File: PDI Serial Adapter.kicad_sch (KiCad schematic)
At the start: 7 parts, among them J1 2.54, J2 1.27, J3 PROG, J4 FTDI, J5 FTDI_VCC, J6 DTR_RST, J7 TARGET_PWR

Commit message: Removed RX/TX from programmer header
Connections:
- net MCU_RX: no longer J3.3 (Pin_3)
- net MCU_TX: no longer J3.4 (Pin_4)
- no-connect marks 1 -> 3
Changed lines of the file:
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@@
     (comment 2 "Licence: GPLv3")
   )
+  (no_connect (at 95.25 88.9))
   (no_connect (at 135.89 68.58))
+  (no_connect (at 107.95 88.9))
   (wire (pts (xy 127 76.2) (xy 135.89 76.2))
     (stroke (width 0) (type default))
@@
     (stroke (width 0) (type default))
   )
-  (wire (pts (xy 86.36 88.9) (xy 95.25 88.9))
-    (stroke (width 0) (type default))
-  )
   (wire (pts (xy 107.95 86.36) (xy 116.84 86.36))
     (stroke (width 0) (type default))
@@
   )
   (wire (pts (xy 107.95 54.61) (xy 116.84 54.61))
-    (stroke (width 0) (type default))
-  )
-  (wire (pts (xy 107.95 88.9) (xy 116.84 88.9))
     (stroke (width 0) (type default))
   )
@@
     (effects (font (size 1.27 1.27)) (justify left bottom))
   )
-  (label "MCU_TX" (at 116.84 88.9 180) (fields_autoplaced)
-    (effects (font (size 1.27 1.27)) (justify right bottom))
-  )
   (label "VCC" (at 116.84 54.61 180) (fields_autoplaced)
     (effects (font (size 1.27 1.27)) (justify right bottom))
@@
     (effects (font (size 1.27 1.27)) (justify left bottom))
   )
-  (label "MCU_RX" (at 86.36 88.9 0) (fields_autoplaced)
-    (effects (font (size 1.27 1.27)) (justify left bottom))
-  )

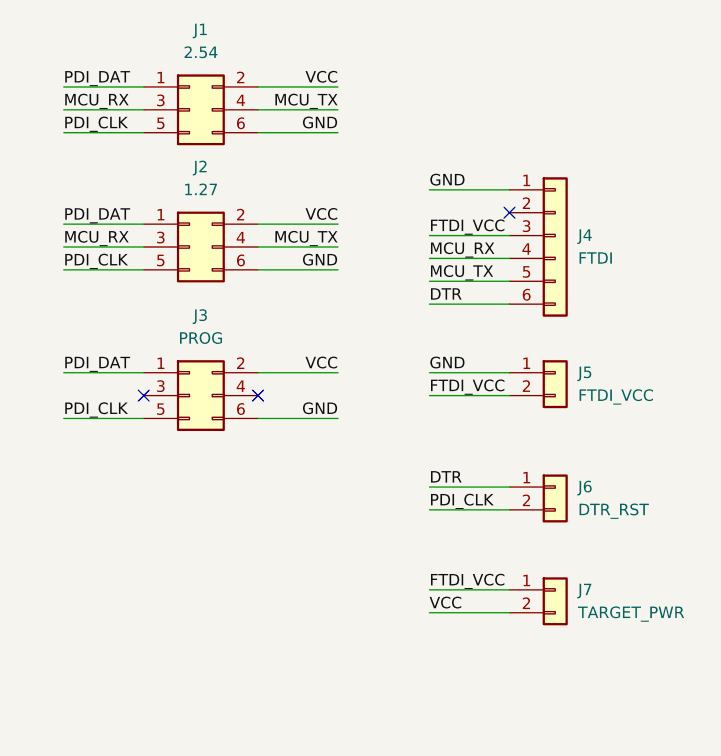
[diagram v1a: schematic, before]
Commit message: Open drain for DTR reset
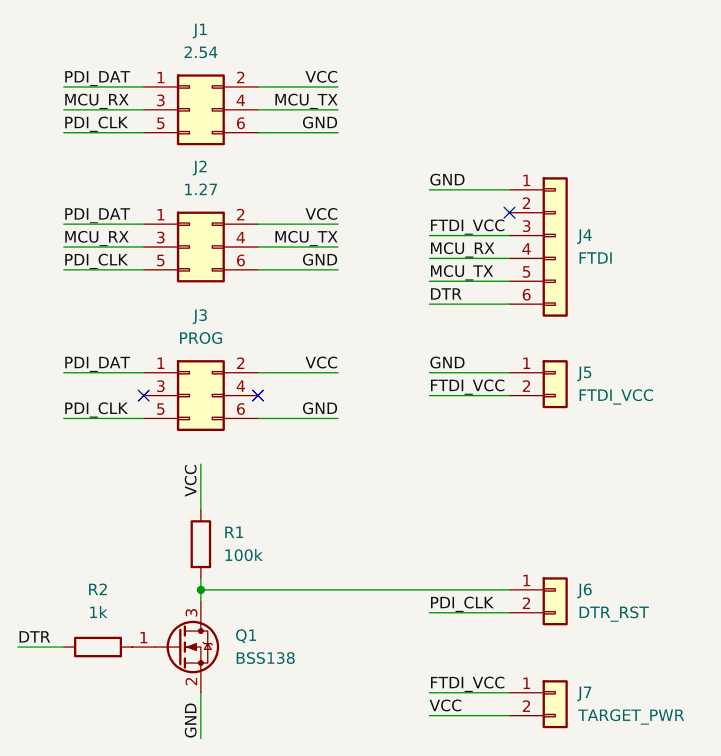
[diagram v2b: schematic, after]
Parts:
- added Q1: BSS138, Package_TO_SOT_SMD:SOT-23, symbol Transistor_FET:BSS138
- added R1: 100k, Resistor_SMD:R_0805_2012Metric_Pad1.20x1.40mm_HandSolder, symbol Device:R
- added R2: 1k, Resistor_SMD:R_0805_2012Metric_Pad1.20x1.40mm_HandSolder, symbol Device:R
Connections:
- net DTR: now also R2.1; no longer J6.1 (Pin_1)
- net GND: now also Q1.2 (S)
- net VCC: now also R1.1
- new net: J6.1 (Pin_1), Q1.3 (D), R1.2
- new net: Q1.1 (G), R2.2
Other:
- moved on the sheet: J6, J7
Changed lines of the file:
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@@
     (comment 2 "Licence: GPLv3")
+  )
+  (junction (at 101.6 110.49) (diameter 0) (color 0 0 0 0)
   )
   (no_connect (at 95.25 88.9))
@@
     (stroke (width 0) (type default))
   )
-  (wire (pts (xy 127 99.06) (xy 135.89 99.06))
-    (stroke (width 0) (type default))
-  )
   (wire (pts (xy 107.95 72.39) (xy 116.84 72.39))
     (stroke (width 0) (type default))
@@
     (stroke (width 0) (type default))
   )
+  (wire (pts (xy 81.28 116.84) (xy 86.36 116.84))
+    (stroke (width 0) (type default))
+  )
   (wire (pts (xy 86.36 57.15) (xy 95.25 57.15))
     (stroke (width 0) (type default))
@@
     (stroke (width 0) (type default))
   )
-  (wire (pts (xy 127 110.49) (xy 135.89 110.49))
+  (wire (pts (xy 127 121.92) (xy 135.89 121.92))
     (stroke (width 0) (type default))
   )
@@
     (stroke (width 0) (type default))
   )
+  (wire (pts (xy 101.6 110.49) (xy 101.6 111.76))
+    (stroke (width 0) (type default))
+  )
   (wire (pts (xy 127 66.04) (xy 135.89 66.04))
     (stroke (width 0) (type default))
@@
     (stroke (width 0) (type default))
   )
+  (wire (pts (xy 101.6 121.92) (xy 101.6 127))
+    (stroke (width 0) (type default))
+  )
+  (wire (pts (xy 101.6 109.22) (xy 101.6 110.49))
+    (stroke (width 0) (type default))
+  )
   (wire (pts (xy 127 78.74) (xy 135.89 78.74))
     (stroke (width 0) (type default))
   )
+  (wire (pts (xy 101.6 96.52) (xy 101.6 101.6))
+    (stroke (width 0) (type default))
+  )
   (wire (pts (xy 86.36 74.93) (xy 95.25 74.93))
     (stroke (width 0) (type default))
@@
     (stroke (width 0) (type default))
   )
+  (wire (pts (xy 127 124.46) (xy 135.89 124.46))
+    (stroke (width 0) (type default))
+  )
   (wire (pts (xy 127 113.03) (xy 135.89 113.03))
     (stroke (width 0) (type default))
   )
-  (wire (pts (xy 127 101.6) (xy 135.89 101.6))
+  (wire (pts (xy 101.6 110.49) (xy 135.89 110.49))
     (stroke (width 0) (type default))
   )
@@
     (effects (font (size 1.27 1.27)) (justify right bottom))
   )
-  (label "PDI_CLK" (at 127 101.6 0) (fields_autoplaced)
-    (effects (font (size 1.27 1.27)) (justify left bottom))
-  )
-  (label "DTR" (at 127 99.06 0) (fields_autoplaced)
+  (label "PDI_CLK" (at 127 113.03 0) (fields_autoplaced)
+    (effects (font (size 1.27 1.27)) (justify left bottom))
+  )
+  (label "DTR" (at 81.28 116.84 0) (fields_autoplaced)
     (effects (font (size 1.27 1.27)) (justify left bottom))
   )
@@
     (effects (font (size 1.27 1.27)) (justify left bottom))
   )
+  (label "GND" (at 101.6 127 90) (fields_autoplaced)
+    (effects (font (size 1.27 1.27)) (justify left bottom))
+  )
   (label "GND" (at 116.84 74.93 180) (fields_autoplaced)
     (effects (font (size 1.27 1.27)) (justify right bottom))
@@
     (effects (font (size 1.27 1.27)) (justify left bottom))
   )
+  (label "VCC" (at 101.6 96.52 270) (fields_autoplaced)
+    (effects (font (size 1.27 1.27)) (justify right bottom))
+  )
   (label "MCU_TX" (at 116.84 72.39 180) (fields_autoplaced)
     (effects (font (size 1.27 1.27)) (justify right bottom))
@@
     (effects (font (size 1.27 1.27)) (justify right bottom))
   )
-  (label "FTDI_VCC" (at 127 110.49 0) (fields_autoplaced)
-    (effects (font (size 1.27 1.27)) (justify left bottom))
-  )
-  (label "VCC" (at 127 113.03 0) (fields_autoplaced)
+  (label "FTDI_VCC" (at 127 121.92 0) (fields_autoplaced)
+    (effects (font (size 1.27 1.27)) (justify left bottom))
+  )
+  (label "VCC" (at 127 124.46 0) (fields_autoplaced)
     (effects (font (size 1.27 1.27)) (justify left bottom))
   )
   (label "GND" (at 127 86.36 0) (fields_autoplaced)
     (effects (font (size 1.27 1.27)) (justify left bottom))
+  )
+  (symbol (lib_id "Device:R") (at 101.6 105.41 0) (unit 1)
+    (in_bom yes) (on_board yes) (dnp no) (fields_autoplaced)
+    (property "Reference" "R1" (at 104.14 104.14 0)
+      (effects (font (size 1.27 1.27)) (justify left))
+    )
+    (property "Value" "100k" (at 104.14 106.68 0)
+      (effects (font (size 1.27 1.27)) (justify left))
+    )
+    (property "Footprint" "Resistor_SMD:R_0805_2012Metric_Pad1.20x1.40mm_HandSolder" (at 99.822 105.41 90)
+      (effects (font (size 1.27 1.27)) hide)
+    )
+    (property "Datasheet" "~" (at 101.6 105.41 0)
+      (effects (font (size 1.27 1.27)) hide)
+    )
+    (pin "1")
+    (pin "2")
+    (instances
+      (project "PDI Serial Adapter"
+        (path "/53f06091-c417-4bfd-9c07-d86260f24dc3"
+          (reference "R1") (unit 1)
+        )
+      )
+    )
   )
   (symbol (lib_id "Connector_Generic:Conn_02x03_Odd_Even") (at 100.33 57.15 0) (unit 1)
@@
     )
   )
+  (symbol (lib_id "Device:R") (at 90.17 116.84 90) (unit 1)
+    (in_bom yes) (on_board yes) (dnp no) (fields_autoplaced)
+    (property "Reference" "R2" (at 90.17 110.49 90)
+      (effects (font (size 1.27 1.27)))
+    )
+    (property "Value" "1k" (at 90.17 113.03 90)
+      (effects (font (size 1.27 1.27)))
+    )
+    (property "Footprint" "Resistor_SMD:R_0805_2012Metric_Pad1.20x1.40mm_HandSolder" (at 90.17 118.618 90)
+      (effects (font (size 1.27 1.27)) hide)
+    )
+    (property "Datasheet" "~" (at 90.17 116.84 0)
+      (effects (font (size 1.27 1.27)) hide)
+    )
+    (pin "1")
+    (pin "2")
+    (instances
+      (project "PDI Serial Adapter"
+        (path "/53f06091-c417-4bfd-9c07-d86260f24dc3"
+          (reference "R2") (unit 1)
+        )
+      )
+    )
+  )
+  (symbol (lib_id "Transistor_FET:BSS138") (at 99.06 116.84 0) (unit 1)
+    (in_bom yes) (on_board yes) (dnp no) (fields_autoplaced)
+    (property "Reference" "Q1" (at 105.41 115.57 0)
+      (effects (font (size 1.27 1.27)) (justify left))
+    )
+    (property "Value" "BSS138" (at 105.41 118.11 0)
+      (effects (font (size 1.27 1.27)) (justify left))
+    )
+    (property "Footprint" "Package_TO_SOT_SMD:SOT-23" (at 104.14 118.745 0)
+      (effects (font (size 1.27 1.27) italic) (justify left) hide)
+    )
+    (property "Datasheet" "https://www.onsemi.com/pub/Collateral/BSS138-D.PDF" (at 99.06 116.84 0)
+      (effects (font (size 1.27 1.27)) (justify left) hide)
+    )
+    (pin "1")
+    (pin "2")
+    (pin "3")
+    (instances
+      (project "PDI Serial Adapter"
+        (path "/53f06091-c417-4bfd-9c07-d86260f24dc3"
+          (reference "Q1") (unit 1)
+        )
+      )
+    )
+  )
   (symbol (lib_id "Connector_Generic:Conn_02x03_Odd_Even") (at 100.33 72.39 0) (unit 1)
     (in_bom yes) (on_board yes) (dnp no) (fields_autoplaced)
@@
     )
   )
-  (symbol (lib_id "Connector_Generic:Conn_01x02") (at 140.97 99.06 0) (unit 1)
-    (in_bom yes) (on_board yes) (dnp no) (fields_autoplaced)
-    (property "Reference" "J6" (at 143.51 99.06 0)
-      (effects (font (size 1.27 1.27)) (justify left))
-    )
-    (property "Value" "DTR_RST" (at 143.51 101.6 0)
-      (effects (font (size 1.27 1.27)) (justify left))
-    )
-    (property "Footprint" "Connector_PinHeader_2.54mm:PinHeader_1x02_P2.54mm_Vertical" (at 140.97 99.06 0)
-      (effects (font (size 1.27 1.27)) hide)
-    )
-    (property "Datasheet" "~" (at 140.97 99.06 0)
+  (symbol (lib_id "Connector_Generic:Conn_01x02") (at 140.97 110.49 0) (unit 1)
+    (in_bom yes) (on_board yes) (dnp no) (fields_autoplaced)
+    (property "Reference" "J6" (at 143.51 110.49 0)
+      (effects (font (size 1.27 1.27)) (justify left))
+    )
+    (property "Value" "DTR_RST" (at 143.51 113.03 0)
+      (effects (font (size 1.27 1.27)) (justify left))
+    )
+    (property "Footprint" "Connector_PinHeader_2.54mm:PinHeader_1x02_P2.54mm_Vertical" (at 140.97 110.49 0)
+      (effects (font (size 1.27 1.27)) hide)
+    )
+    (property "Datasheet" "~" (at 140.97 110.49 0)
       (effects (font (size 1.27 1.27)) hide)
     )
@@
     )
   )
-  (symbol (lib_id "Connector_Generic:Conn_01x02") (at 140.97 110.49 0) (unit 1)
-    (in_bom yes) (on_board yes) (dnp no) (fields_autoplaced)
-    (property "Reference" "J7" (at 143.51 110.49 0)
-      (effects (font (size 1.27 1.27)) (justify left))
-    )
-    (property "Value" "TARGET_PWR" (at 143.51 113.03 0)
-      (effects (font (size 1.27 1.27)) (justify left))
-    )
-    (property "Footprint" "Connector_PinHeader_2.54mm:PinHeader_1x02_P2.54mm_Vertical" (at 140.97 110.49 0)
-      (effects (font (size 1.27 1.27)) hide)
-    )
-    (property "Datasheet" "~" (at 140.97 110.49 0)
-      (effects (font (size 1.27 1.27)) hide)
-    )
+  (symbol (lib_id "Connector_Generic:Conn_01x02") (at 140.97 121.92 0) (unit 1)
+    (in_bom yes) (on_board yes) (dnp no) (fields_autoplaced)
+    (property "Reference" "J7" (at 143.51 121.92 0)
+      (effects (font (size 1.27 1.27)) (justify left))
+    )
+    (property "Value" "TARGET_PWR" (at 143.51 124.46 0)
+      (effects (font (size 1.27 1.27)) (justify left))
+    )
+    (property "Footprint" "Connector_PinHeader_2.54mm:PinHeader_1x02_P2.54mm_Vertical" (at 140.97 121.92 0)
+      (effects (font (size 1.27 1.27)) hide)
+    )
+    (property "Datasheet" "~" (at 140.97 121.92 0)
+      (effects (font (size 1.27 1.27)) hide)
+    )
